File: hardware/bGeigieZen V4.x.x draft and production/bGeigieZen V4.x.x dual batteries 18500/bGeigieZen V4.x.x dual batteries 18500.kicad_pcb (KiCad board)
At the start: 2 copper layers, 129.4 x 64.6 mm, 11 parts, among them J1 M5 2x15 pin, J2 Geiger IRover, J3 GPS, J4 Geiger Safepulse, J5 Extra support header

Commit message: hardware board V4.0.4 updates
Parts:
- moved G front 32.0 mm to (158.3, 100.8), turned to 90 degrees
- moved J3 27.1 mm to (183.8, 105.1)
- moved BT2 0.96 mm to (203.9, 99.1)
- turned G back to 180 degrees
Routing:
- net /SCL: track 46.0 -> 72.7 mm
- net /SDA: track 38.7 -> 63.9 mm
- net /RX2: track 41.5 -> 63.5 mm
- net /TX2: track 41.9 -> 63.5 mm
- net /GIO2 on Core and GIO32 on Core-2: track 106.1 -> 109.8 mm
- net 3.3V: track 96.1 -> 97.0 mm

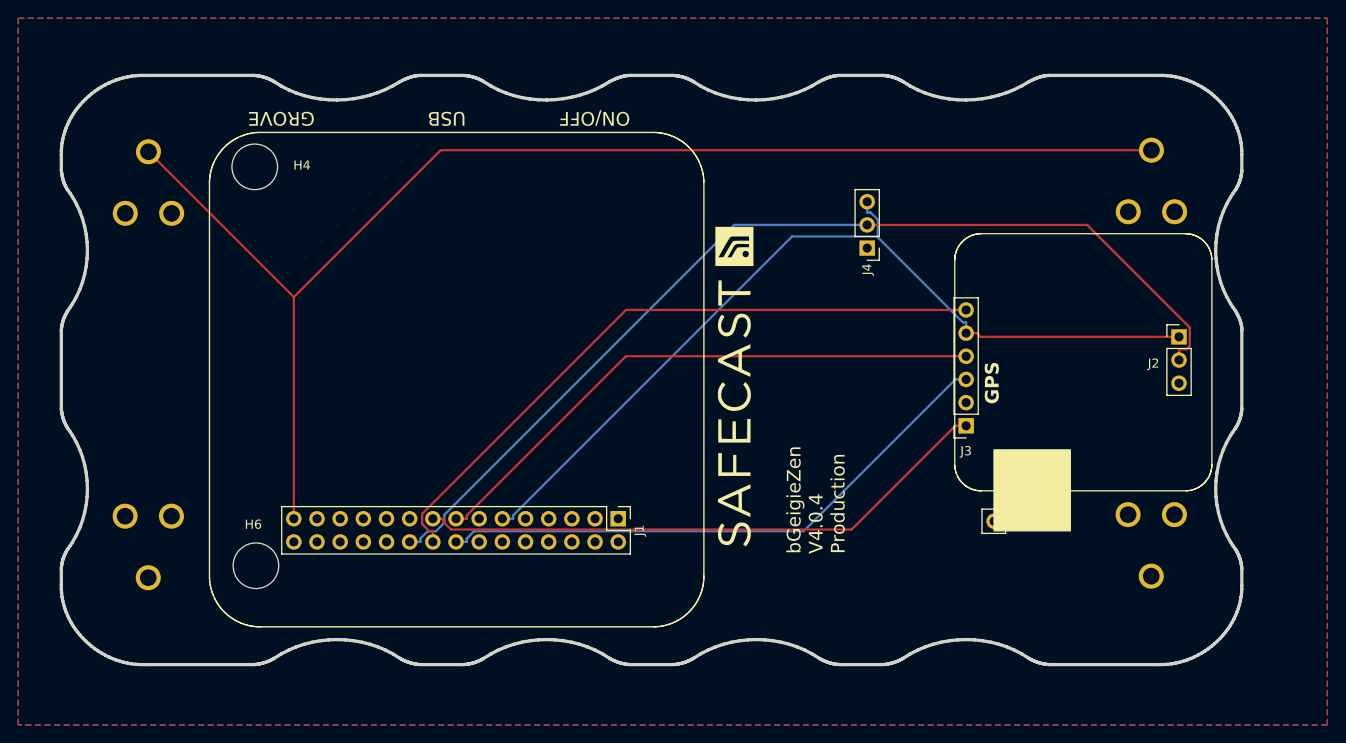
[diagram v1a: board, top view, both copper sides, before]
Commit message: Added LiPo charger connector
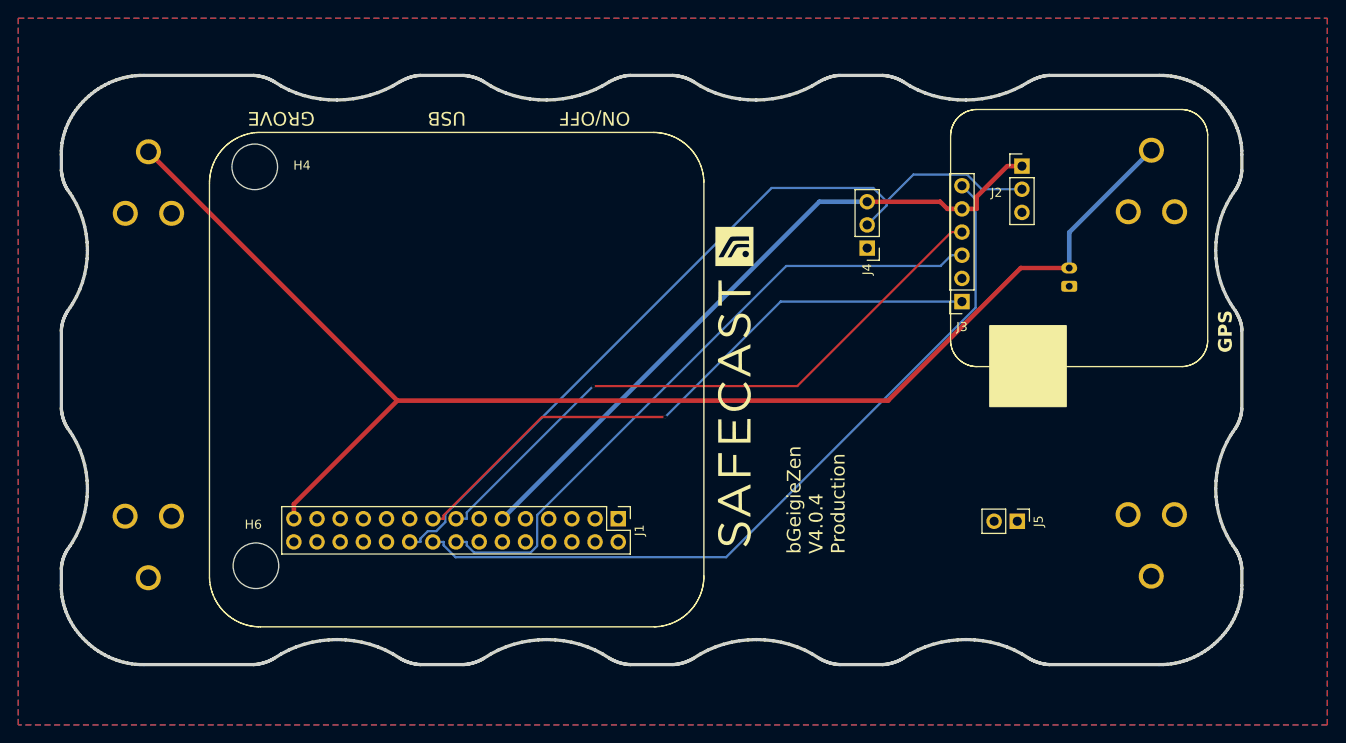
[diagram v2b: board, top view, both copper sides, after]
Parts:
- added J6: LiPo charger, Connector_JST:JST_PH_B2B-PH-K_1x02_P2.00mm_Vertical, B.Cu at (195.1, 89.8)
- moved J2 25.4 mm to (189.9, 76.6)
- moved J3 13.6 mm to (183.3, 91.5)
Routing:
- net 3.3V: track 97.0 -> 74.4 mm
- net /GIO2 on Core and GIO32 on Core-2: track 109.8 -> 89.9 mm
- net /SCL: track 72.7 -> 85.7 mm
- net /TX2: track 63.5 -> 71.7 mm
- net /RX2: track 63.5 -> 68.9 mm, vias 0 -> 1
- net /BAT: track 147.5 -> 152.6 mm
- net /SDA: track 63.9 -> 68.1 mm, vias 0 -> 1

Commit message: Small fixed on 4.0.4 board
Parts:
- moved BT2 1.68 mm to (202.2, 99.0)
- moved BT1 1.65 mm to (95.7, 105.2)
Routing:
- net /BAT: track 152.6 -> 152.0 mm

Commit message: More updates 4.0.4 boards
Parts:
- added G***: LOGO, bGeigieRaku_M5_1015:18650 map, B.Cu at (95.7, 103.0)
- added G***: LOGO, bGeigieRaku_M5_1015:18650 map, B.Cu at (202.5, 103.2)
- J6: value LiPo charger -> Charger
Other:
- board text added: "+"
- board text added: "-"
- board text added: "M5StackCore"
